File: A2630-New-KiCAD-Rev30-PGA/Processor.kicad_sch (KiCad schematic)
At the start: 59 parts, among them J202 25/FPU, U200 MC68030, U201 MC68882, U204 74AHCT04, X1 25MHz, X2 25MHz

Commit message: Add files via upload
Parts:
- added R238: 68, Resistor_SMD:R_0805_2012Metric, symbol Device:R
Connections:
- net _BERR: now also R238.1; no longer U200.69 (BERR)
- new net: R238.2, U200.69 (BERR)
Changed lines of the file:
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@@
   (title_block
     (title "Amiga N2630")
-    (date "2022-12-01")
+    (date "2022-12-04")
     (rev "3.0")
   )
@@
     (stroke (width 0) (type default) (color 0 0 0 0))
   )
-  (wire (pts (xy 177.165 93.98) (xy 29.21 93.98))
+  (wire (pts (xy 177.165 93.98) (xy 162.052 93.98))
     (stroke (width 0) (type default) (color 0 0 0 0))
   )
@@
     (stroke (width 0) (type default) (color 0 0 0 0))
   )
+  (wire (pts (xy 154.432 93.98) (xy 29.21 93.98))
+    (stroke (width 0) (type default) (color 0 0 0 0))
+  )
   (wire (pts (xy 332.74 89.535) (xy 332.74 48.895))
     (stroke (width 0) (type default) (color 0 0 0 0))
@@
     (pin "9")
   )
+  (symbol (lib_id "Device:R") (at 158.242 93.98 90) (unit 1)
+    (in_bom yes) (on_board yes)
+    (property "Reference" "R238" (id 0) (at 158.242 95.885 90))
+    (property "Value" "68" (id 1) (at 158.242 93.98 90))
+    (property "Footprint" "Resistor_SMD:R_0805_2012Metric" (id 2) (at 158.242 95.758 90)
+      (effects (font (size 1.27 1.27)) hide)
+    )
+    (property "Datasheet" "~" (id 3) (at 158.242 93.98 0)
+      (effects (font (size 1.27 1.27)) hide)
+    )
+    (pin "1")
+    (pin "2")
+  )
   (symbol (lib_id "74xx:74LS04") (at 88.265 189.2554 0) (unit 2)

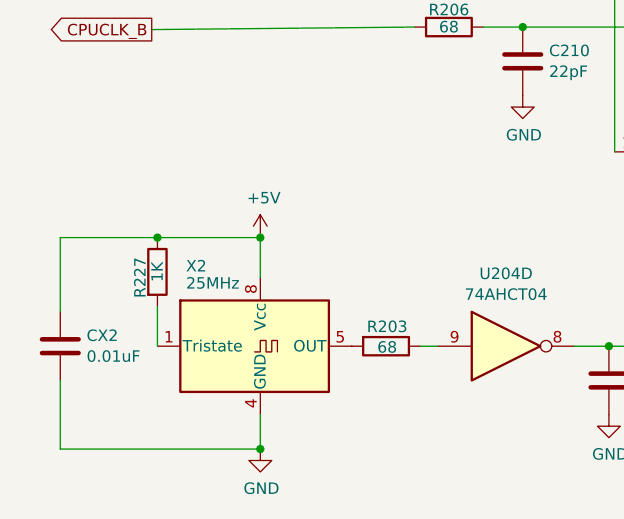
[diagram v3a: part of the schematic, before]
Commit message: Exclude non-BOM items.
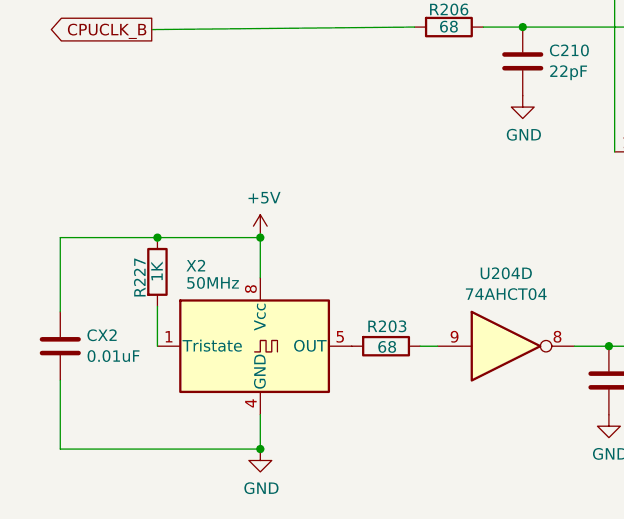
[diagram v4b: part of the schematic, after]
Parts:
- X2: value 25MHz -> 50MHz
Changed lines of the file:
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@@
   (title_block
     (title "Amiga N2630")
-    (date "2022-12-04")
+    (date "2023-01-23")
     (rev "3.0")
   )
@@
       (effects (font (size 1.27 1.27)) (justify left))
     )
-    (property "Value" "25MHz" (id 1) (at 33.02 234.95 0)
+    (property "Value" "50MHz" (id 1) (at 33.02 234.95 0)
       (effects (font (size 1.27 1.27)) (justify left))
     )
